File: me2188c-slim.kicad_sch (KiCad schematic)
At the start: 5 parts, among them J1 Conn_01x04_Male, U1 ME2188

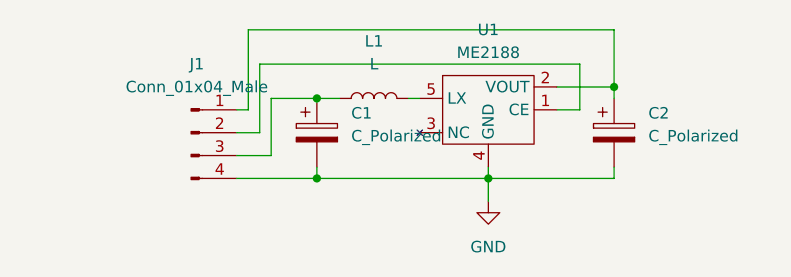
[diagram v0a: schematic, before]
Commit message: inductor footprint corrected and capacitors added
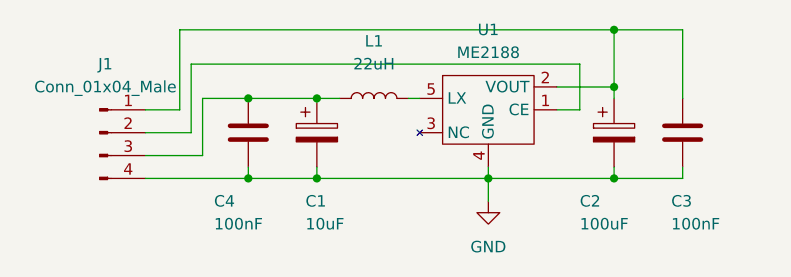
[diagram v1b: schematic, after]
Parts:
- added C3, C4: 100nF, Capacitor_SMD:C_0805_2012Metric_Pad1.18x1.45mm_HandSolder, symbol Device:C
- C1: value C_Polarized -> 10uF
- C2: value C_Polarized -> 100uF
- L1: value L -> 22uH; footprint Inductor_SMD:L_Coilcraft_XAL60xx_6.36x6.56mm -> Inductor_SMD:L_Ferrocore_DLG-0403
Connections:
- net GND: now also C3.2, C4.2
- net at C2.1, J1.1 (Pin_1), U1.2 (VOUT): now also C3.1
- net at C1.1, J1.3 (Pin_3), L1.1: now also C4.1
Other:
- moved on the sheet: J1
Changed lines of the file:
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@@
   (junction (at 138.43 90.17) (diameter 0) (color 0 0 0 0)
   )
+  (junction (at 171.45 82.55) (diameter 0) (color 0 0 0 0)
+  )
+  (junction (at 130.81 99.06) (diameter 0) (color 0 0 0 0)
+  )
+  (junction (at 171.45 99.06) (diameter 0) (color 0 0 0 0)
+  )
   (junction (at 138.43 99.06) (diameter 0) (color 0 0 0 0)
   )
   (junction (at 171.45 88.9) (diameter 0) (color 0 0 0 0)
   )
+  (junction (at 130.81 90.17) (diameter 0) (color 0 0 0 0)
+  )
   (wire (pts (xy 157.48 97.79) (xy 157.48 99.06))
     (stroke (width 0) (type default) (color 0 0 0 0))
@@
     (stroke (width 0) (type default) (color 0 0 0 0))
   )
+  (wire (pts (xy 130.81 99.06) (xy 138.43 99.06))
+    (stroke (width 0) (type default) (color 0 0 0 0))
+  )
   (wire (pts (xy 138.43 99.06) (xy 157.48 99.06))
     (stroke (width 0) (type default) (color 0 0 0 0))
@@
     (stroke (width 0) (type default) (color 0 0 0 0))
   )
+  (wire (pts (xy 130.81 90.17) (xy 138.43 90.17))
+    (stroke (width 0) (type default) (color 0 0 0 0))
+  )
   (wire (pts (xy 171.45 99.06) (xy 171.45 97.79))
     (stroke (width 0) (type default) (color 0 0 0 0))
   )
-  (wire (pts (xy 133.35 90.17) (xy 138.43 90.17))
+  (wire (pts (xy 125.73 90.17) (xy 130.81 90.17))
+    (stroke (width 0) (type default) (color 0 0 0 0))
+  )
+  (wire (pts (xy 130.81 97.79) (xy 130.81 99.06))
     (stroke (width 0) (type default) (color 0 0 0 0))
   )
@@
     (stroke (width 0) (type default) (color 0 0 0 0))
   )
-  (wire (pts (xy 130.81 82.55) (xy 130.81 91.44))
+  (wire (pts (xy 123.19 82.55) (xy 123.19 91.44))
     (stroke (width 0) (type default) (color 0 0 0 0))
   )
@@
     (stroke (width 0) (type default) (color 0 0 0 0))
   )
-  (wire (pts (xy 130.81 91.44) (xy 129.54 91.44))
-    (stroke (width 0) (type default) (color 0 0 0 0))
-  )
-  (wire (pts (xy 133.35 96.52) (xy 133.35 90.17))
-    (stroke (width 0) (type default) (color 0 0 0 0))
-  )
-  (wire (pts (xy 129.54 96.52) (xy 133.35 96.52))
-    (stroke (width 0) (type default) (color 0 0 0 0))
-  )
-  (wire (pts (xy 132.08 86.36) (xy 132.08 93.98))
+  (wire (pts (xy 123.19 91.44) (xy 119.38 91.44))
+    (stroke (width 0) (type default) (color 0 0 0 0))
+  )
+  (wire (pts (xy 125.73 96.52) (xy 125.73 90.17))
+    (stroke (width 0) (type default) (color 0 0 0 0))
+  )
+  (wire (pts (xy 119.38 96.52) (xy 125.73 96.52))
+    (stroke (width 0) (type default) (color 0 0 0 0))
+  )
+  (wire (pts (xy 124.46 86.36) (xy 124.46 93.98))
+    (stroke (width 0) (type default) (color 0 0 0 0))
+  )
+  (wire (pts (xy 179.07 99.06) (xy 171.45 99.06))
     (stroke (width 0) (type default) (color 0 0 0 0))
   )
@@
     (stroke (width 0) (type default) (color 0 0 0 0))
   )
-  (wire (pts (xy 171.45 82.55) (xy 130.81 82.55))
-    (stroke (width 0) (type default) (color 0 0 0 0))
-  )
-  (wire (pts (xy 129.54 99.06) (xy 138.43 99.06))
+  (wire (pts (xy 179.07 97.79) (xy 179.07 99.06))
+    (stroke (width 0) (type default) (color 0 0 0 0))
+  )
+  (wire (pts (xy 171.45 82.55) (xy 123.19 82.55))
+    (stroke (width 0) (type default) (color 0 0 0 0))
+  )
+  (wire (pts (xy 119.38 99.06) (xy 130.81 99.06))
     (stroke (width 0) (type default) (color 0 0 0 0))
   )
@@
     (stroke (width 0) (type default) (color 0 0 0 0))
   )
-  (wire (pts (xy 167.64 86.36) (xy 132.08 86.36))
-    (stroke (width 0) (type default) (color 0 0 0 0))
-  )
-  (wire (pts (xy 132.08 93.98) (xy 129.54 93.98))
-    (stroke (width 0) (type default) (color 0 0 0 0))
+  (wire (pts (xy 179.07 82.55) (xy 171.45 82.55))
+    (stroke (width 0) (type default) (color 0 0 0 0))
+  )
+  (wire (pts (xy 167.64 86.36) (xy 124.46 86.36))
+    (stroke (width 0) (type default) (color 0 0 0 0))
+  )
+  (wire (pts (xy 124.46 93.98) (xy 119.38 93.98))
+    (stroke (width 0) (type default) (color 0 0 0 0))
+  )
+  (wire (pts (xy 179.07 82.55) (xy 179.07 90.17))
+    (stroke (width 0) (type default) (color 0 0 0 0))
+  )
+  (symbol (lib_id "Device:C") (at 179.07 93.98 0) (unit 1)
+    (in_bom yes) (on_board yes)
+    (property "Reference" "C3" (id 0) (at 177.8 101.6 0)
+      (effects (font (size 1.27 1.27)) (justify left))
+    )
+    (property "Value" "100nF" (id 1) (at 177.8 104.14 0)
+      (effects (font (size 1.27 1.27)) (justify left))
+    )
+    (property "Footprint" "Capacitor_SMD:C_0805_2012Metric_Pad1.18x1.45mm_HandSolder" (id 2) (at 180.0352 97.79 0)
+      (effects (font (size 1.27 1.27)) hide)
+    )
+    (property "Datasheet" "~" (id 3) (at 179.07 93.98 0)
+      (effects (font (size 1.27 1.27)) hide)
+    )
+    (pin "1")
+    (pin "2")
+  )
+  (symbol (lib_id "Device:C") (at 130.81 93.98 0) (unit 1)
+    (in_bom yes) (on_board yes)
+    (property "Reference" "C4" (id 0) (at 127 101.6 0)
+      (effects (font (size 1.27 1.27)) (justify left))
+    )
+    (property "Value" "100nF" (id 1) (at 127 104.14 0)
+      (effects (font (size 1.27 1.27)) (justify left))
+    )
+    (property "Footprint" "Capacitor_SMD:C_0805_2012Metric_Pad1.18x1.45mm_HandSolder" (id 2) (at 131.7752 97.79 0)
+      (effects (font (size 1.27 1.27)) hide)
+    )
+    (property "Datasheet" "~" (id 3) (at 130.81 93.98 0)
+      (effects (font (size 1.27 1.27)) hide)
+    )
+    (pin "1")
+    (pin "2")
   )
   (symbol (lib_id "Converter_mini_DCDC:ME2188") (at 157.48 90.17 0) (unit 1)
@@
     (pin "5")
   )
-  (symbol (lib_id "Connector:Conn_01x04_Male") (at 124.46 93.98 0) (unit 1)
-    (in_bom yes) (on_board yes) (fields_autoplaced)
-    (property "Reference" "J1" (id 0) (at 125.095 86.36 0))
-    (property "Value" "Conn_01x04_Male" (id 1) (at 125.095 88.9 0))
-    (property "Footprint" "Connector_PinHeader_2.54mm:PinHeader_1x04_P2.54mm_Vertical" (id 2) (at 124.46 93.98 0)
-      (effects (font (size 1.27 1.27)) hide)
-    )
-    (property "Datasheet" "~" (id 3) (at 124.46 93.98 0)
+  (symbol (lib_id "Connector:Conn_01x04_Male") (at 114.3 93.98 0) (unit 1)
+    (in_bom yes) (on_board yes) (fields_autoplaced)
+    (property "Reference" "J1" (id 0) (at 114.935 86.36 0))
+    (property "Value" "Conn_01x04_Male" (id 1) (at 114.935 88.9 0))
+    (property "Footprint" "Connector_PinHeader_2.54mm:PinHeader_1x04_P2.54mm_Vertical" (id 2) (at 114.3 93.98 0)
+      (effects (font (size 1.27 1.27)) hide)
+    )
+    (property "Datasheet" "~" (id 3) (at 114.3 93.98 0)
       (effects (font (size 1.27 1.27)) hide)
     )
@@
   )
   (symbol (lib_id "Device:C_Polarized") (at 138.43 93.98 0) (unit 1)
-    (in_bom yes) (on_board yes) (fields_autoplaced)
-    (property "Reference" "C1" (id 0) (at 142.24 91.8209 0)
-      (effects (font (size 1.27 1.27)) (justify left))
-    )
-    (property "Value" "C_Polarized" (id 1) (at 142.24 94.3609 0)
+    (in_bom yes) (on_board yes)
+    (property "Reference" "C1" (id 0) (at 137.16 101.6 0)
+      (effects (font (size 1.27 1.27)) (justify left))
+    )
+    (property "Value" "10uF" (id 1) (at 137.16 104.14 0)
       (effects (font (size 1.27 1.27)) (justify left))
     )
@@
     (in_bom yes) (on_board yes) (fields_autoplaced)
     (property "Reference" "L1" (id 0) (at 144.78 83.82 90))
-    (property "Value" "L" (id 1) (at 144.78 86.36 90))
-    (property "Footprint" "Inductor_SMD:L_Coilcraft_XAL60xx_6.36x6.56mm" (id 2) (at 144.78 90.17 0)
+    (property "Value" "22uH" (id 1) (at 144.78 86.36 90))
+    (property "Footprint" "Inductor_SMD:L_Ferrocore_DLG-0403" (id 2) (at 144.78 90.17 0)
       (effects (font (size 1.27 1.27)) hide)
     )
@@
   )
   (symbol (lib_id "Device:C_Polarized") (at 171.45 93.98 0) (unit 1)
-    (in_bom yes) (on_board yes) (fields_autoplaced)
-    (property "Reference" "C2" (id 0) (at 175.26 91.8209 0)
-      (effects (font (size 1.27 1.27)) (justify left))
-    )
-    (property "Value" "C_Polarized" (id 1) (at 175.26 94.3609 0)
+    (in_bom yes) (on_board yes)
+    (property "Reference" "C2" (id 0) (at 167.64 101.6 0)
+      (effects (font (size 1.27 1.27)) (justify left))
+    )
+    (property "Value" "100uF" (id 1) (at 167.64 104.14 0)
       (effects (font (size 1.27 1.27)) (justify left))
     )
@@
     )
     (path "/7a1b224c-c27e-4fc4-91ba-362036528311"
-      (reference "C1") (unit 1) (value "C_Polarized") (footprint "Capacitor_Tantalum_SMD:CP_EIA-7343-31_Kemet-D_Pad2.25x2.55mm_HandSolder")
+      (reference "C1") (unit 1) (value "10uF") (footprint "Capacitor_Tantalum_SMD:CP_EIA-7343-31_Kemet-D_Pad2.25x2.55mm_HandSolder")
     )
     (path "/d4f9d6cc-f9d1-4c70-ae6e-79c207960817"
-      (reference "C2") (unit 1) (value "C_Polarized") (footprint "Capacitor_Tantalum_SMD:CP_EIA-7343-31_Kemet-D_Pad2.25x2.55mm_HandSolder")
+      (reference "C2") (unit 1) (value "100uF") (footprint "Capacitor_Tantalum_SMD:CP_EIA-7343-31_Kemet-D_Pad2.25x2.55mm_HandSolder")
+    )
+    (path "/1e1acdca-faa0-4e52-893c-6a6e7bf15788"
+      (reference "C3") (unit 1) (value "100nF") (footprint "Capacitor_SMD:C_0805_2012Metric_Pad1.18x1.45mm_HandSolder")
+    )
+    (path "/1fb0fca5-35a7-42b0-8e0a-6c912466520a"
+      (reference "C4") (unit 1) (value "100nF") (footprint "Capacitor_SMD:C_0805_2012Metric_Pad1.18x1.45mm_HandSolder")
     )
     (path "/5e60f2e5-cf20-4885-bd94-1872bceb0c12"
@@
     )
     (path "/b49cd461-77e3-432c-ac4b-891fcbd77c26"
-      (reference "L1") (unit 1) (value "L") (footprint "Inductor_SMD:L_Coilcraft_XAL60xx_6.36x6.56mm")
+      (reference "L1") (unit 1) (value "22uH") (footprint "Inductor_SMD:L_Ferrocore_DLG-0403")
     )
     (path "/2c1310ad-2f46-419f-8785-a6d66fab433c"

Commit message: shrinked and routed
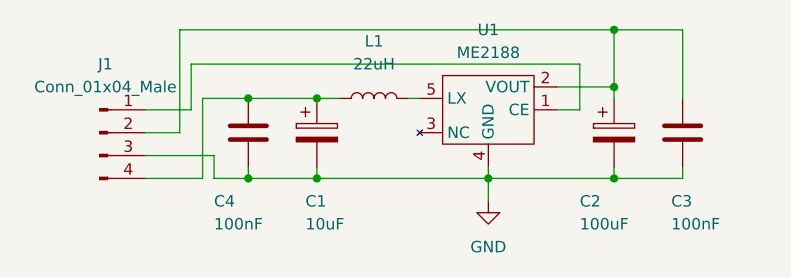
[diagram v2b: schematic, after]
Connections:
- net GND: now also J1.3 (Pin_3); no longer J1.4 (Pin_4)
- net at C2.1, C3.1, U1.2 (VOUT): now also J1.2 (Pin_2); no longer J1.1 (Pin_1)
- net at C1.1, C4.1, L1.1: now also J1.4 (Pin_4); no longer J1.3 (Pin_3)
- net at U1.1 (CE): now also J1.1 (Pin_1); no longer J1.2 (Pin_2)
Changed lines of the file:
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@@
 (kicad_sch (version 20211123) (generator eeschema)
   (paper "A4")
+  (junction (at 130.81 99.06) (diameter 0) (color 0 0 0 0)
+  )
   (junction (at 157.48 99.06) (diameter 0) (color 0 0 0 0)
   )
@@
   )
   (junction (at 171.45 82.55) (diameter 0) (color 0 0 0 0)
-  )
-  (junction (at 130.81 99.06) (diameter 0) (color 0 0 0 0)
   )
   (junction (at 171.45 99.06) (diameter 0) (color 0 0 0 0)
@@
     (stroke (width 0) (type default) (color 0 0 0 0))
   )
-  (wire (pts (xy 130.81 99.06) (xy 138.43 99.06))
+  (wire (pts (xy 127 99.06) (xy 130.81 99.06))
     (stroke (width 0) (type default) (color 0 0 0 0))
   )
@@
     (stroke (width 0) (type default) (color 0 0 0 0))
   )
+  (wire (pts (xy 119.38 99.06) (xy 125.73 99.06))
+    (stroke (width 0) (type default) (color 0 0 0 0))
+  )
   (wire (pts (xy 165.1 88.9) (xy 171.45 88.9))
+    (stroke (width 0) (type default) (color 0 0 0 0))
+  )
+  (wire (pts (xy 119.38 93.98) (xy 123.19 93.98))
+    (stroke (width 0) (type default) (color 0 0 0 0))
+  )
+  (wire (pts (xy 127 99.06) (xy 127 96.52))
     (stroke (width 0) (type default) (color 0 0 0 0))
   )
@@
     (stroke (width 0) (type default) (color 0 0 0 0))
   )
-  (wire (pts (xy 123.19 82.55) (xy 123.19 91.44))
-    (stroke (width 0) (type default) (color 0 0 0 0))
-  )
   (wire (pts (xy 138.43 97.79) (xy 138.43 99.06))
     (stroke (width 0) (type default) (color 0 0 0 0))
@@
     (stroke (width 0) (type default) (color 0 0 0 0))
   )
-  (wire (pts (xy 123.19 91.44) (xy 119.38 91.44))
+  (wire (pts (xy 127 96.52) (xy 119.38 96.52))
     (stroke (width 0) (type default) (color 0 0 0 0))
   )
-  (wire (pts (xy 125.73 96.52) (xy 125.73 90.17))
-    (stroke (width 0) (type default) (color 0 0 0 0))
-  )
-  (wire (pts (xy 119.38 96.52) (xy 125.73 96.52))
-    (stroke (width 0) (type default) (color 0 0 0 0))
-  )
-  (wire (pts (xy 124.46 86.36) (xy 124.46 93.98))
+  (wire (pts (xy 124.46 86.36) (xy 124.46 91.44))
     (stroke (width 0) (type default) (color 0 0 0 0))
   )
@@
     (stroke (width 0) (type default) (color 0 0 0 0))
   )
-  (wire (pts (xy 119.38 99.06) (xy 130.81 99.06))
+  (wire (pts (xy 138.43 90.17) (xy 140.97 90.17))
     (stroke (width 0) (type default) (color 0 0 0 0))
   )
-  (wire (pts (xy 138.43 90.17) (xy 140.97 90.17))
+  (wire (pts (xy 125.73 90.17) (xy 125.73 99.06))
     (stroke (width 0) (type default) (color 0 0 0 0))
   )
@@
     (stroke (width 0) (type default) (color 0 0 0 0))
   )
-  (wire (pts (xy 124.46 93.98) (xy 119.38 93.98))
+  (wire (pts (xy 123.19 82.55) (xy 123.19 93.98))
     (stroke (width 0) (type default) (color 0 0 0 0))
   )
+  (wire (pts (xy 130.81 99.06) (xy 138.43 99.06))
+    (stroke (width 0) (type default) (color 0 0 0 0))
+  )
+  (wire (pts (xy 119.38 91.44) (xy 124.46 91.44))
+    (stroke (width 0) (type default) (color 0 0 0 0))
+  )
